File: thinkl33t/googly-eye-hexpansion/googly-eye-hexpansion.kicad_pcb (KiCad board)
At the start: 2 copper layers, 49 x 38 mm, 12 parts, among them J1 Hexpansion-Connector, U1 ZD24C64A-XGMT

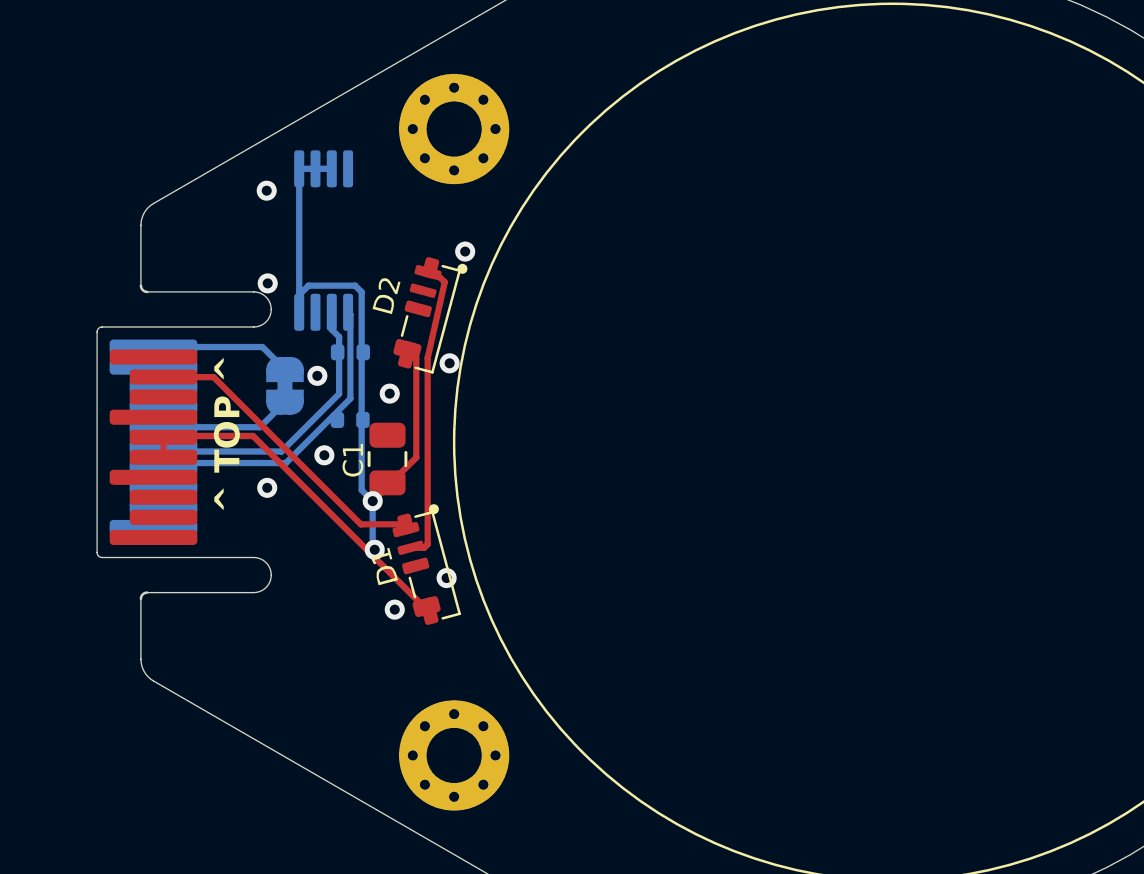
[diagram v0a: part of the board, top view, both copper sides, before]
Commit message: Add ap3602 to boost from 3v3 to 5v, as the minimum for the LEDs is 3.5v
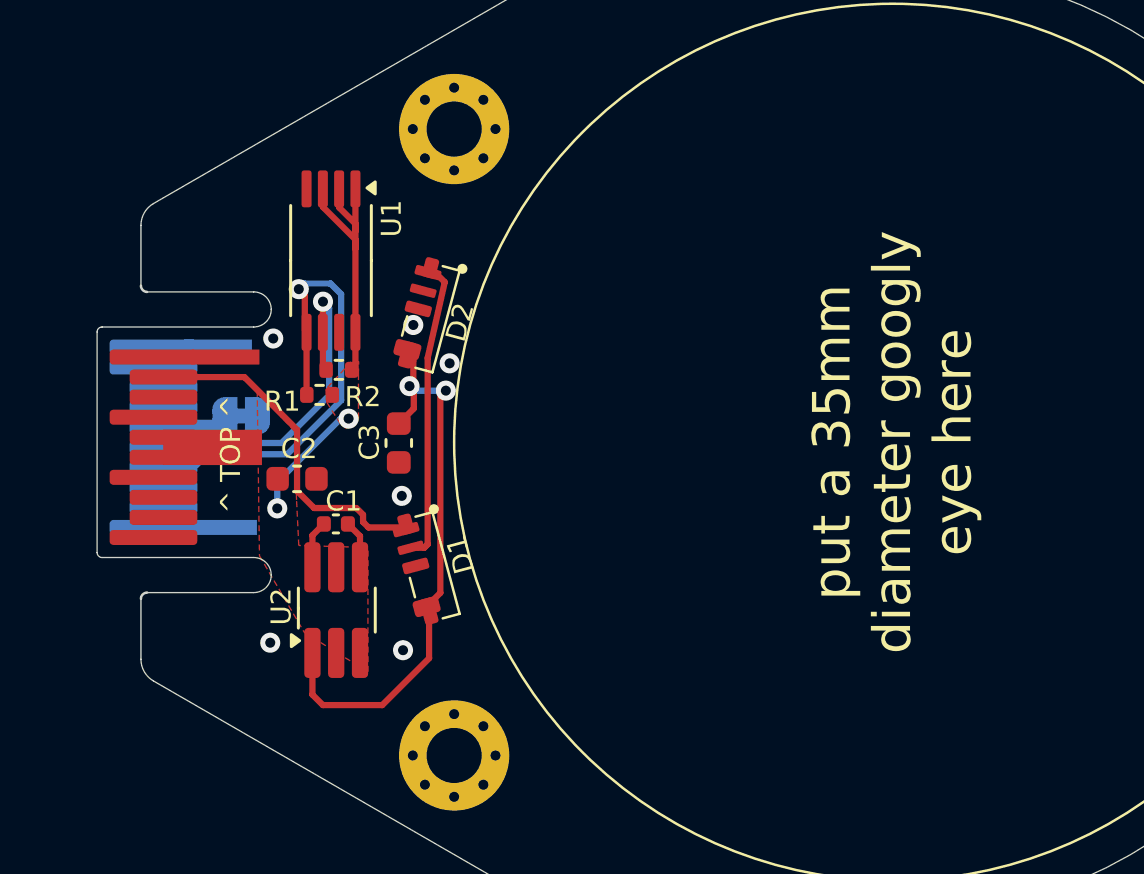
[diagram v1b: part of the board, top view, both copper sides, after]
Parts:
- added C2: 10uF, Capacitor_SMD:C_0603_1608Metric, F.Cu at (106.2, 101.5)
- added C3: 10uF, Capacitor_SMD:C_0603_1608Metric, F.Cu at (110.3, 100.0)
- added U2: AP3602A, Package_TO_SOT_SMD:TSOT-23-6_HandSoldering, F.Cu at (107.8, 106.7)
- C1: value 100nF -> 1uF; footprint Capacitor_SMD:C_0805_2012Metric -> Capacitor_SMD:C_0402_1005Metric
- R1, R2, U1: moved to F.Cu
- moved C1 3.31 mm to (107.8, 103.3), turned to 0 degrees
- moved JP1 2.12 mm to (104.0, 99.0), turned to 0 degrees
- moved R1 1.58 mm to (107.1, 98.1)
- moved U1 0.85 mm to (107.6, 92.8)
- moved R2 0.84 mm to (107.9, 97.1)
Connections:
- C1 pad 1: /GND -> Net-(U2-C+)
- C1 pad 2: /3V3 -> Net-(U2-C-)
- D1 pad 1: /3V3 -> /5V
- D2 pad 1: /3V3 -> /5V
- J1 pad 13: /HS_G -> unconnected-(J1-HS_G-Pad13)
- J1 pad 18: /HS_H -> unconnected-(J1-HS_H-Pad18)
- J1 pad 19: /HS_I -> unconnected-(J1-HS_I-Pad19)
- J1 pad 2: /LS_A -> unconnected-(J1-LS_A-Pad2)
- J1 pad 3: /LS_B -> unconnected-(J1-LS_B-Pad3)
- J1 pad 7: /LS_C -> unconnected-(J1-LS_C-Pad7)
- J1 pad 8: /LS_D -> unconnected-(J1-LS_D-Pad8)
- J1 pad 9: /LS_E -> unconnected-(J1-LS_E-Pad9)
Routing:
- net /3V3: track 42.0 -> 17.3 mm
- net /5V: track 0.00 -> 23.0 mm, vias 0 -> 2
- net /GND: track 5.62 -> 0.00 mm, vias 10 -> 6
- net /SDA: track 12.1 -> 17.4 mm, vias 0 -> 1
- net /HEXP_DET: track 5.26 -> 0.00 mm
- net /SCL: track 11.4 -> 13.7 mm, vias 0 -> 1
- net Net-(U2-C-): track 0.00 -> 1.93 mm
- net Net-(U2-C+): track 0.00 -> 1.92 mm
- net /HS_F: track 12.1 -> 13.8 mm
- added copper zone on F.Cu, net /3V3
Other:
- board text added: "This is the googly eye hexpansion that i have made for the 2024 emf badge. It turns out the back of this is huge so i can put so much text on it, good isn't it! (c) 2024 Bob Clough v2.0"
- board text added: "put a 35mm diameter googly eye here"
